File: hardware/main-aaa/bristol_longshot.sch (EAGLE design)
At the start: 57 parts, among them U1 SAM_D20E, U2 SI4060, U3 UBLOX_MAX, U4 ADP1607ACPZN-R7, U5 TG-5006CJ, U6 TG-5006CJ, U7 TPS3123, U8 SN74LVC1G32DCKR, U9 SE880, Y1 ABS05

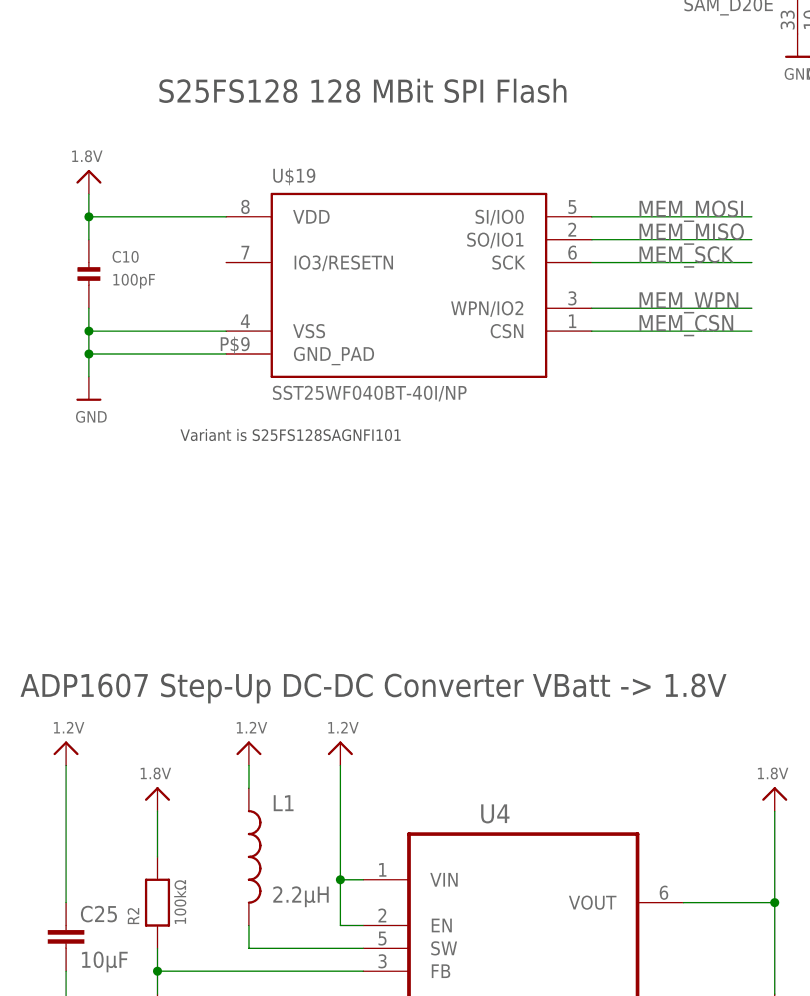
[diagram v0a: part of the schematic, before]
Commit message: Updated many parts lists, updated bard numbering, removed makefiles for inactive things
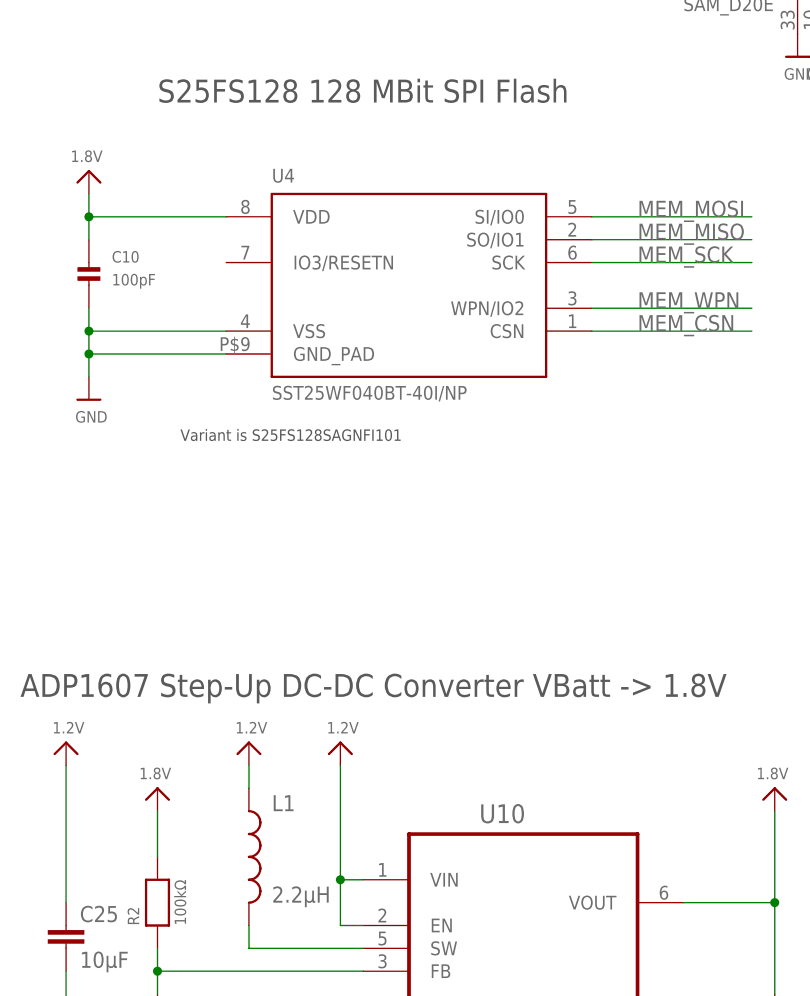
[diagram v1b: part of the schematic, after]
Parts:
- removed U$19: SST25WF040BT-40I/NP, fbri:SST25WF040BT-40I/NP
- added U10: ADP1607ACPZN-R7, ADP1607:ADP1607ACPZN-R7
- U4: value ADP1607ACPZN-R7 -> SST25WF040BT-40I/NP; device ADP1607:ADP1607ACPZN-R7 -> fbri:SST25WF040BT-40I/NP
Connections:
- net 1.2V: now also U10.EN, U10.VIN; no longer U4.EN, U4.VIN
- net 1.8V: now also U10.VOUT, U4.VDD; no longer U$19.VDD, U4.VOUT
- net FB: now also U10.FB; no longer U4.FB
- net GND: now also U10.EP, U10.GND, U4.GND_PAD, U4.VSS; no longer U$19.GND_PAD, U$19.VSS, U4.EP, U4.GND
- net MEM_CSN: now also U4.CSN; no longer U$19.CSN
- net MEM_MISO: now also U4.SO/IO1; no longer U$19.SO/IO1
- net MEM_MOSI: now also U4.SI/IO0; no longer U$19.SI/IO0
- net MEM_SCK: now also U4.SCK; no longer U$19.SCK
- net MEM_WPN: now also U4.WPN/IO2; no longer U$19.WPN/IO2
- net SW: now also U10.SW; no longer U4.SW
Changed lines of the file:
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@@
 <part name="C17" library="microbuilder_v3" deviceset="CAP_CERAMIC" device="_0402" value="100nF"/>
 <part name="U$78" library="microbuilder_v3" deviceset="GND" device=""/>
-<part name="U$19" library="fbri" deviceset="SST25WF040BT-40I/NP" device=""/>
+<part name="U4" library="fbri" deviceset="SST25WF040BT-40I/NP" device=""/>
 <part name="FRAME4" library="SparkFun" deviceset="FRAME-LETTER" device=""/>
 <part name="U$22" library="microbuilder_v3" deviceset="GND" device=""/>
@@
 <part name="U$51" library="microbuilder_v3" deviceset="1.2V" device=""/>
 <part name="C24" library="resistor" deviceset="C-EU" device="C0603K" value="10µF"/>
-<part name="U4" library="ADP1607" deviceset="ADP1607ACPZN-R7" device=""/>
+<part name="U10" library="ADP1607" deviceset="ADP1607ACPZN-R7" device=""/>
 <part name="U$55" library="microbuilder_v3" deviceset="1.2V" device=""/>
 <part name="R2" library="microbuilder_v3" deviceset="RESISTOR" device="_0402" value="100kΩ"/>
@@
 <instance part="C17" gate="G$1" x="12.7" y="121.92"/>
 <instance part="U$78" gate="G$1" x="12.7" y="114.3"/>
-<instance part="U$19" gate="G$1" x="101.6" y="25.4"/>
+<instance part="U4" gate="G$1" x="101.6" y="25.4"/>
 <instance part="FRAME4" gate="G$1" x="0" y="-187.96"/>
 <instance part="FRAME4" gate="G$2" x="144.78" y="-187.96"/>
@@
 <instance part="U$51" gate="G$1" x="33.02" y="-33.02"/>
 <instance part="C24" gate="G$1" x="142.24" y="-55.88"/>
-<instance part="U4" gate="A" x="114.3" y="-45.72"/>
+<instance part="U10" gate="A" x="114.3" y="-45.72"/>
 <instance part="U$55" gate="G$1" x="83.82" y="-25.4"/>
 <instance part="R2" gate="G$1" x="73.66" y="-43.18" rot="R90"/>
@@
 <wire x1="66.04" y1="20.32" x2="66.04" y2="22.86" width="0.1524" layer="91"/>
 <junction x="66.04" y="20.32"/>
-<pinref part="U$19" gate="G$1" pin="VSS"/>
-<pinref part="U$19" gate="G$1" pin="GND_PAD"/>
+<pinref part="U4" gate="G$1" pin="VSS"/>
+<pinref part="U4" gate="G$1" pin="GND_PAD"/>
 </segment>
 <segment>
@@
 </segment>
 <segment>
-<pinref part="U4" gate="A" pin="GND"/>
+<pinref part="U10" gate="A" pin="GND"/>
 <pinref part="U$22" gate="G$1" pin="GND"/>
 <wire x1="96.52" y1="-55.88" x2="93.98" y2="-55.88" width="0.1524" layer="91"/>
 <wire x1="93.98" y1="-55.88" x2="93.98" y2="-58.42" width="0.1524" layer="91"/>
-<pinref part="U4" gate="A" pin="EP"/>
+<pinref part="U10" gate="A" pin="EP"/>
 <wire x1="93.98" y1="-58.42" x2="93.98" y2="-66.04" width="0.1524" layer="91"/>
 <wire x1="96.52" y1="-58.42" x2="93.98" y2="-58.42" width="0.1524" layer="91"/>
@@
 <wire x1="66.04" y1="30.48" x2="66.04" y2="33.02" width="0.1524" layer="91"/>
 <junction x="66.04" y="33.02"/>
-<pinref part="U$19" gate="G$1" pin="VDD"/>
+<pinref part="U4" gate="G$1" pin="VDD"/>
 </segment>
 <segment>
@@
 <wire x1="142.24" y1="-53.34" x2="142.24" y2="-43.18" width="0.1524" layer="91"/>
 <pinref part="C24" gate="G$1" pin="1"/>
-<pinref part="U4" gate="A" pin="VOUT"/>
+<pinref part="U10" gate="A" pin="VOUT"/>
 <wire x1="142.24" y1="-43.18" x2="142.24" y2="-33.02" width="0.1524" layer="91"/>
 <wire x1="132.08" y1="-43.18" x2="142.24" y2="-43.18" width="0.1524" layer="91"/>
@@
 <wire x1="121.92" y1="33.02" x2="139.7" y2="33.02" width="0.1524" layer="91"/>
 <label x="127" y="33.02" size="1.778" layer="95" ratio="11"/>
-<pinref part="U$19" gate="G$1" pin="SI/IO0"/>
+<pinref part="U4" gate="G$1" pin="SI/IO0"/>
 </segment>
 <segment>
@@
 <wire x1="139.7" y1="20.32" x2="121.92" y2="20.32" width="0.1524" layer="91"/>
 <label x="127" y="20.32" size="1.778" layer="95" ratio="11"/>
-<pinref part="U$19" gate="G$1" pin="CSN"/>
+<pinref part="U4" gate="G$1" pin="CSN"/>
 </segment>
 <segment>
@@
 <wire x1="121.92" y1="22.86" x2="139.7" y2="22.86" width="0.1524" layer="91"/>
 <label x="127" y="22.86" size="1.778" layer="95" ratio="11"/>
-<pinref part="U$19" gate="G$1" pin="WPN/IO2"/>
+<pinref part="U4" gate="G$1" pin="WPN/IO2"/>
 </segment>
 </net>
@@
 <wire x1="121.92" y1="27.94" x2="139.7" y2="27.94" width="0.1524" layer="91"/>
 <label x="127" y="27.94" size="1.778" layer="95" ratio="11"/>
-<pinref part="U$19" gate="G$1" pin="SCK"/>
+<pinref part="U4" gate="G$1" pin="SCK"/>
 </segment>
 <segment>
@@
 <wire x1="121.92" y1="30.48" x2="139.7" y2="30.48" width="0.1524" layer="91"/>
 <label x="127" y="30.48" size="1.778" layer="95" ratio="11"/>
-<pinref part="U$19" gate="G$1" pin="SO/IO1"/>
+<pinref part="U4" gate="G$1" pin="SO/IO1"/>
 </segment>
 <segment>
@@
 </segment>
 <segment>
-<pinref part="U4" gate="A" pin="VIN"/>
+<pinref part="U10" gate="A" pin="VIN"/>
 <pinref part="U$38" gate="G$1" pin="1.2V"/>
 <wire x1="96.52" y1="-40.64" x2="93.98" y2="-40.64" width="0.1524" layer="91"/>
 <wire x1="93.98" y1="-40.64" x2="93.98" y2="-27.94" width="0.1524" layer="91"/>
-<pinref part="U4" gate="A" pin="EN"/>
+<pinref part="U10" gate="A" pin="EN"/>
 <wire x1="96.52" y1="-45.72" x2="93.98" y2="-45.72" width="0.1524" layer="91"/>
 <wire x1="93.98" y1="-45.72" x2="93.98" y2="-40.64" width="0.1524" layer="91"/>
@@
 <net name="SW" class="0">
 <segment>
-<pinref part="U4" gate="A" pin="SW"/>
+<pinref part="U10" gate="A" pin="SW"/>
 <wire x1="96.52" y1="-48.26" x2="83.82" y2="-48.26" width="0.1524" layer="91"/>
 <pinref part="L1" gate="G$1" pin="2"/>
@@
 <net name="FB" class="0">
 <segment>
-<pinref part="U4" gate="A" pin="FB"/>
+<pinref part="U10" gate="A" pin="FB"/>
 <pinref part="R3" gate="G$1" pin="2"/>
 <wire x1="96.52" y1="-50.8" x2="73.66" y2="-50.8" width="0.1524" layer="91"/>

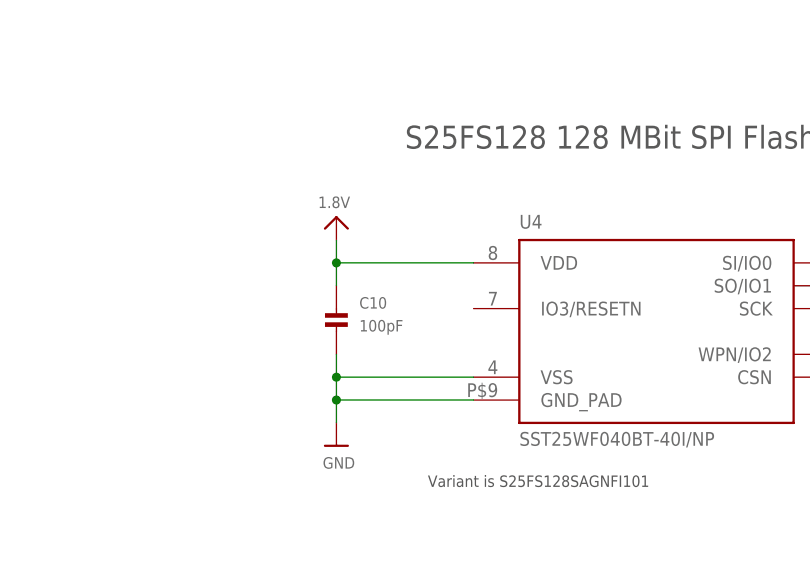
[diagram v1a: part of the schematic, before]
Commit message: [Bugfix] Memory HOLD pin needs to be high. Also adjusted pad/cream size. Bump to V0.98x.1
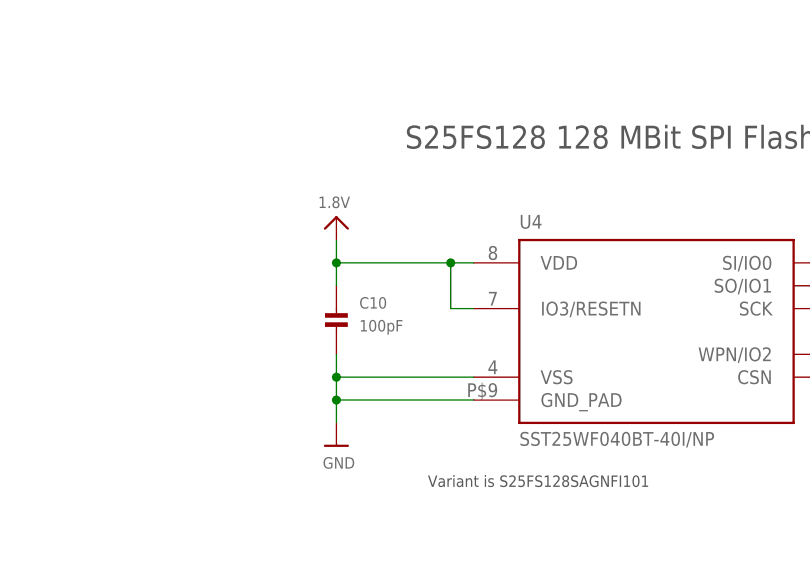
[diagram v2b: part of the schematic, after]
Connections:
- net 1.8V: now also U4.IO3/RESETN
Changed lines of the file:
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@@
 <segment>
 <pinref part="U$40" gate="G$1" pin="1.8V"/>
-<wire x1="81.28" y1="33.02" x2="66.04" y2="33.02" width="0.1524" layer="91"/>
+<wire x1="81.28" y1="33.02" x2="78.74" y2="33.02" width="0.1524" layer="91"/>
+<wire x1="78.74" y1="33.02" x2="66.04" y2="33.02" width="0.1524" layer="91"/>
 <wire x1="66.04" y1="33.02" x2="66.04" y2="35.56" width="0.1524" layer="91"/>
 <pinref part="C10" gate="G$1" pin="P$1"/>
@@
 <junction x="66.04" y="33.02"/>
 <pinref part="U4" gate="G$1" pin="VDD"/>
+<pinref part="U4" gate="G$1" pin="IO3/RESETN"/>
+<wire x1="81.28" y1="27.94" x2="78.74" y2="27.94" width="0.1524" layer="91"/>
+<wire x1="78.74" y1="27.94" x2="78.74" y2="33.02" width="0.1524" layer="91"/>
+<junction x="78.74" y="33.02"/>
 </segment>
 <segment>

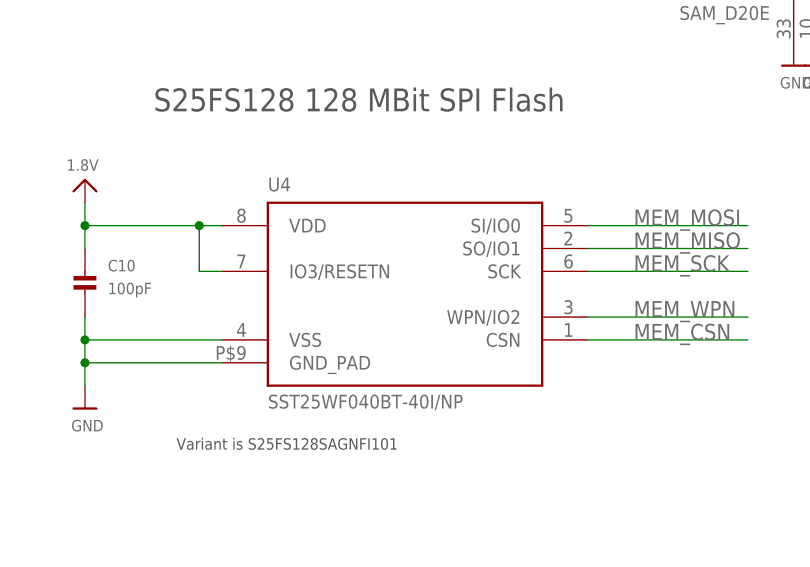
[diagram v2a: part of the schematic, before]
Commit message: Fixed memory pin names to correspond with the datasheet
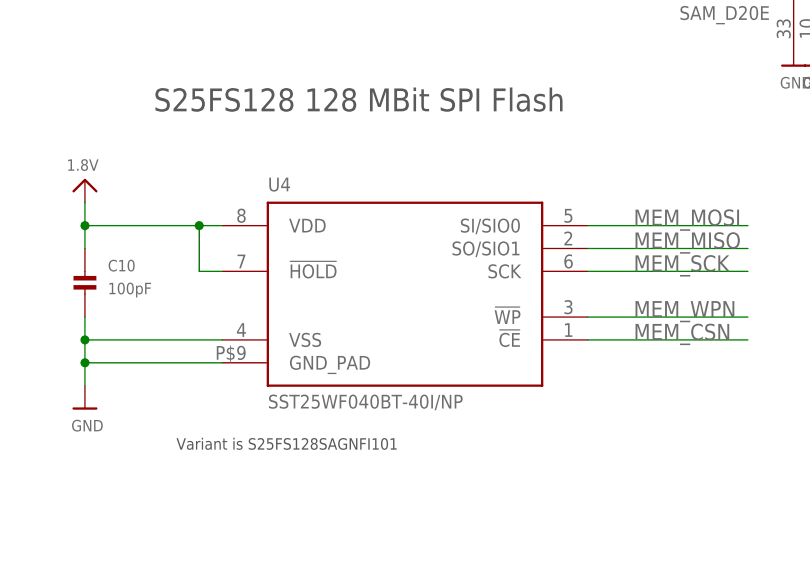
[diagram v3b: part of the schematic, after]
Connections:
- net 1.8V: now also U4.!HOLD; no longer U4.IO3/RESETN
- net MEM_CSN: now also U4.!CE; no longer U4.CSN
- net MEM_MISO: now also U4.SO/SIO1; no longer U4.SO/IO1
- net MEM_MOSI: now also U4.SI/SIO0; no longer U4.SI/IO0
- net MEM_WPN: now also U4.!WP; no longer U4.WPN/IO2
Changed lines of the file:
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@@
 <junction x="66.04" y="33.02"/>
 <pinref part="U4" gate="G$1" pin="VDD"/>
-<pinref part="U4" gate="G$1" pin="IO3/RESETN"/>
+<pinref part="U4" gate="G$1" pin="!HOLD"/>
 <wire x1="81.28" y1="27.94" x2="78.74" y2="27.94" width="0.1524" layer="91"/>
 <wire x1="78.74" y1="27.94" x2="78.74" y2="33.02" width="0.1524" layer="91"/>
@@
 <wire x1="121.92" y1="33.02" x2="139.7" y2="33.02" width="0.1524" layer="91"/>
 <label x="127" y="33.02" size="1.778" layer="95" ratio="11"/>
-<pinref part="U4" gate="G$1" pin="SI/IO0"/>
+<pinref part="U4" gate="G$1" pin="SI/SIO0"/>
 </segment>
 <segment>
@@
 <wire x1="139.7" y1="20.32" x2="121.92" y2="20.32" width="0.1524" layer="91"/>
 <label x="127" y="20.32" size="1.778" layer="95" ratio="11"/>
-<pinref part="U4" gate="G$1" pin="CSN"/>
+<pinref part="U4" gate="G$1" pin="!CE"/>
 </segment>
 <segment>
@@
 <wire x1="121.92" y1="22.86" x2="139.7" y2="22.86" width="0.1524" layer="91"/>
 <label x="127" y="22.86" size="1.778" layer="95" ratio="11"/>
-<pinref part="U4" gate="G$1" pin="WPN/IO2"/>
+<pinref part="U4" gate="G$1" pin="!WP"/>
 </segment>
 </net>
@@
 <wire x1="121.92" y1="30.48" x2="139.7" y2="30.48" width="0.1524" layer="91"/>
 <label x="127" y="30.48" size="1.778" layer="95" ratio="11"/>
-<pinref part="U4" gate="G$1" pin="SO/IO1"/>
-</segment>
-<segment>
+<pinref part="U4" gate="G$1" pin="SO/SIO1"/>
+</segment>
+<segment>
